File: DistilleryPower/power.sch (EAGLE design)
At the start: 31 parts, among them IC2 ACS758LCB-050B-PFF-T, J1 GREEN-2P-5.0, J2 GREEN-2P-5.0, Q1 BC807-16LT1SMD, T1 BT138-DSH, U1 STM32F042KXTX

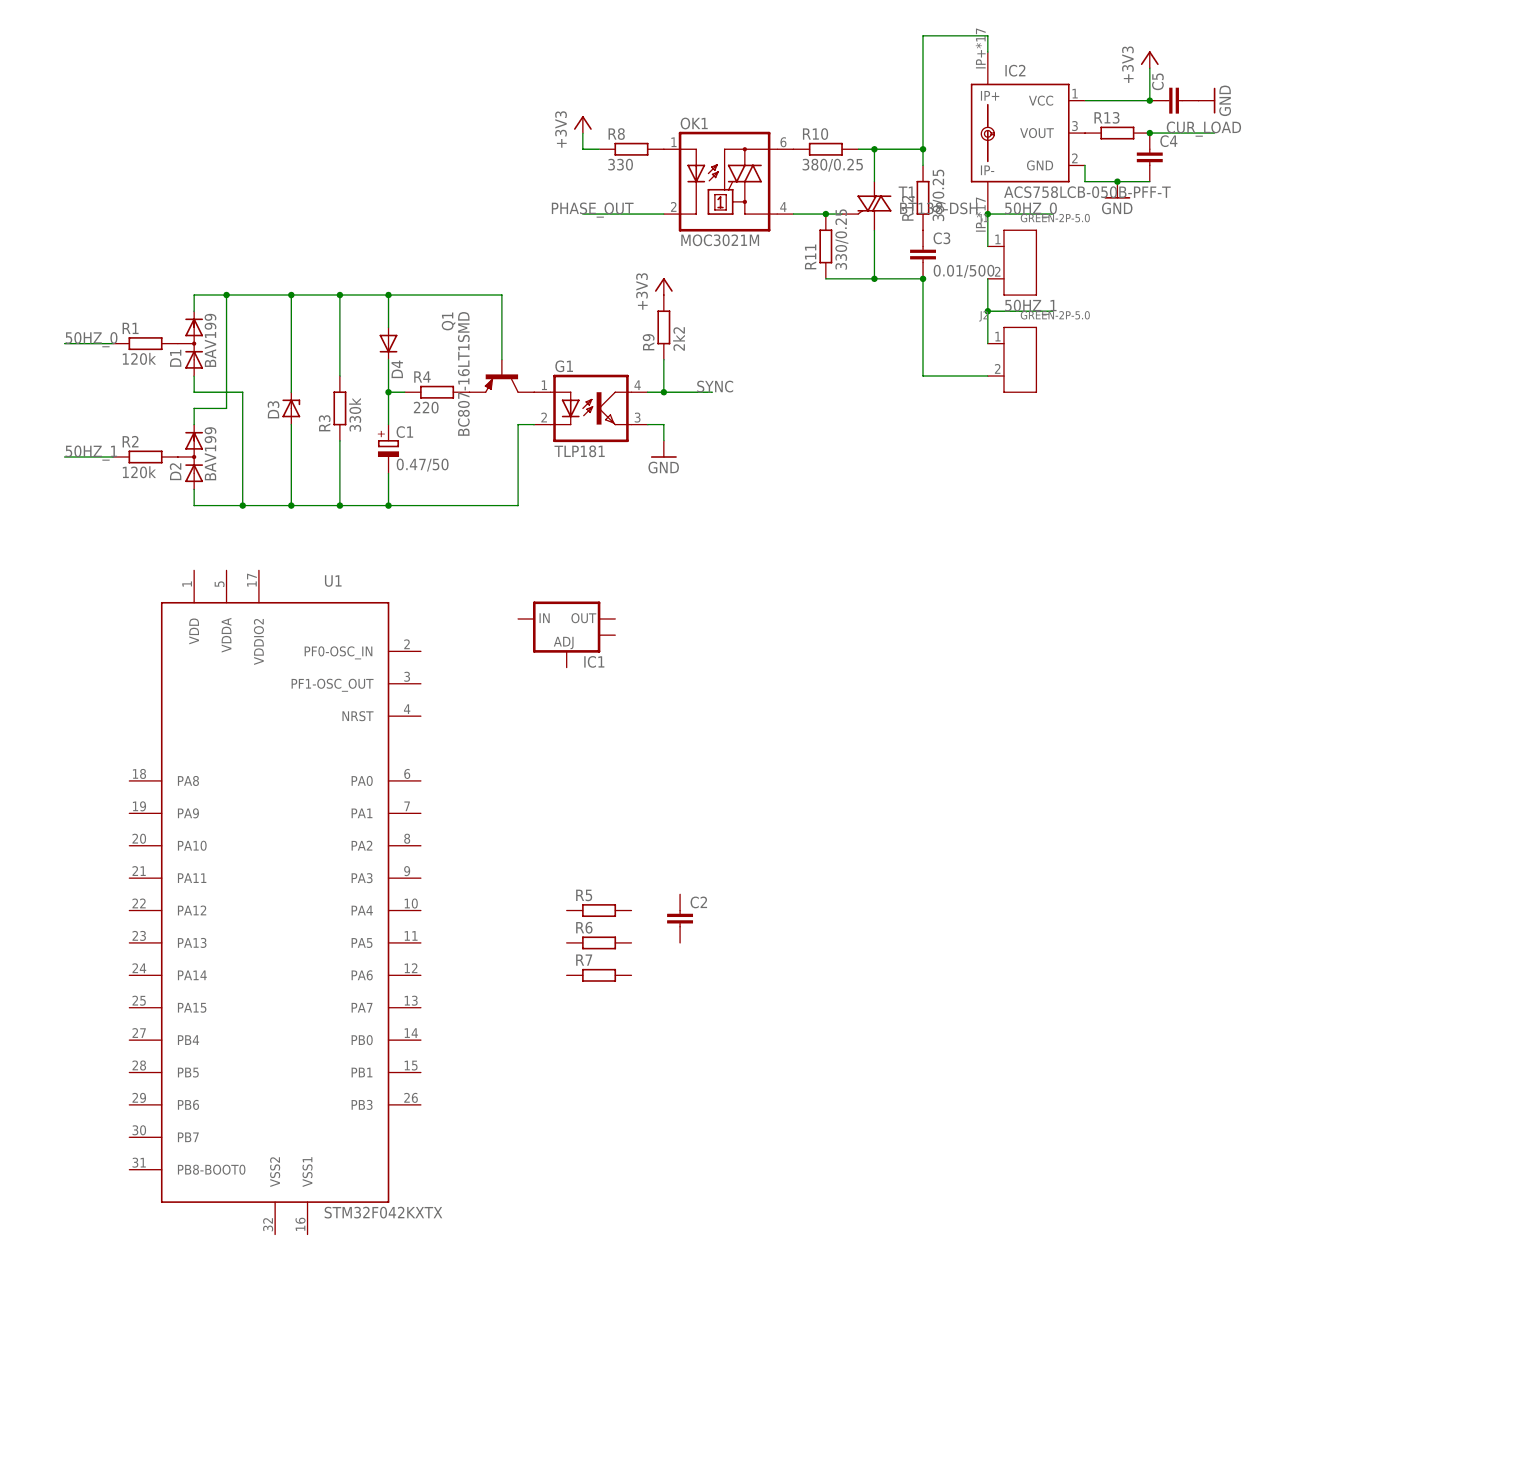
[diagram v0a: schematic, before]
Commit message: digital part schematics
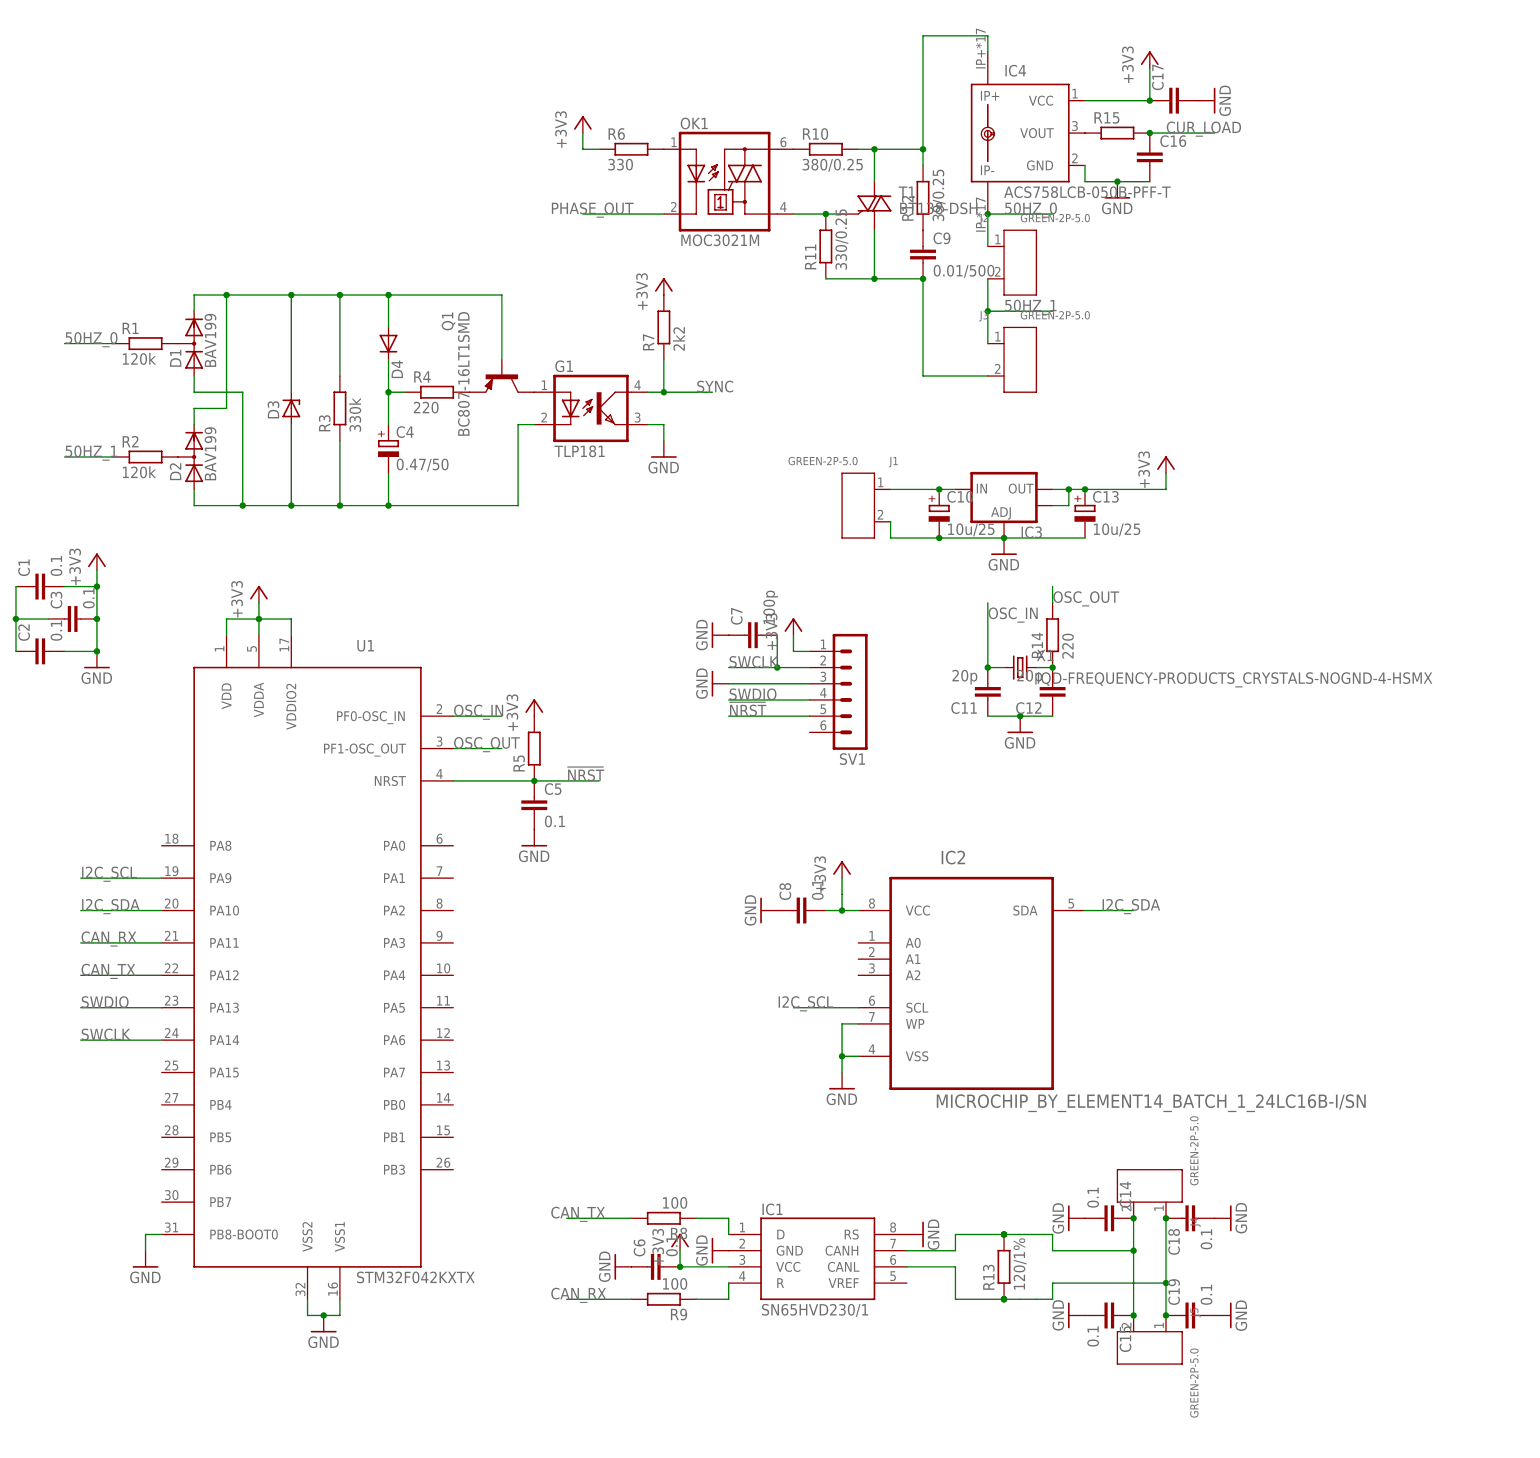
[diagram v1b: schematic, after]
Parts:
- added C10, C13: 10u/25, rcl:CPOL-EUSMCB
- added C11, C12: 20p, rcl:C-EUC0805
- added C14, C15, C18, C19, C6, C8: 0.1, rcl:C-EUC0805
- added C16, C17: (no value), rcl:C-EUC0805
- added C7: 100p, rcl:C-EUC0805
- added C9: 0.01/500, rcl:C-EUC1206
- added IC3: (no value), SparkFun:V_REG_LM1117SOT223
- added IC4: ACS758LCB-050B-PFF-T, allegro:ACS758LCB-050B-PFF-T
- added J3, J4, J5: GREEN-2P-5.0, distillery:SCREW-TERMINAL-GREEN(2P-5.0)
- added R14: 220, rcl:R-EU_R0805
- added R15: (no value), rcl:R-EU_R0805
- added SV1: (no value), distillery:CON-LSTB_MA06-1
- added X1: IQD-FREQUENCY-PRODUCTS_CRYSTALS-NOGND-4-HSMX, distillery:IQD-FREQUENCY-PRODUCTS_CRYSTALS-NOGND-4-HSMX
- C1: value 0.47/50 -> 0.1; device rcl:CPOL-EUC/6032-28R -> rcl:C-EUC0805
- C2, C5: value (none) -> 0.1
- C3: value 0.01/500 -> 0.1; device rcl:C-EUC1206 -> rcl:C-EUC0805
- C4: value (none) -> 0.47/50; device rcl:C-EUC0805 -> rcl:CPOL-EUC/6032-28R
- IC1: value (none) -> SN65HVD230/1; device SparkFun:V_REG_LM1117SOT223 -> distillery:SN65HVD230/1
- IC2: value ACS758LCB-050B-PFF-T -> MICROCHIP_BY_ELEMENT14_BATCH_1_24LC16B-I/SN; device allegro:ACS758LCB-050B-PFF-T -> distillery:MICROCHIP_BY_ELEMENT14_BATCH_1_24LC16B-I/SN
- R13: value (none) -> 120/1%
- R6: value (none) -> 330
- R7: value (none) -> 2k2
- R8: value 330 -> 100
- R9: value 2k2 -> 100
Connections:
- new net !NRST: C5.1, R5.1, SV1.5, U1.NRST
- new net CAN_RX: R9.2, U1.PA11
- new net CAN_TX: R8.2, U1.PA12
- new net I2C_SCL: IC2.SCL, U1.PA9
- new net I2C_SDA: IC2.SDA, U1.PA10
- new net N$13: C10.+, IC3.IN, J1.1
- new net N$16: C12.2, R14.1, X1.2
- new net N$19: C1.1, C2.1, C3.1
- new net N$20: C18.1, C19.1, IC1.CANL, J4.1, J5.1, R13.1
- new net N$21: IC1.D, R8.1
- new net N$22: IC1.R, R9.1
- new net N$24: C14.1, C15.1, IC1.CANH, J4.2, J5.2, R13.2
- new net OSC_IN: C11.2, U1.PF0-OSC_IN, X1.1
- new net OSC_OUT: R14.2, U1.PF1-OSC_OUT
- new net SWCLK: C7.2, SV1.2, U1.PA14
- new net SWDIO: SV1.4, U1.PA13
- net +3V3: now also C13.+, C17.1, C6.2, C8.2, IC1.VCC, IC3.OUT, IC3.OUT@1, IC4.VCC, R5.2, R6.1, R7.2, SV1.1, U1.VDD, U1.VDDA, U1.VDDIO2; no longer C5.1, R8.1, R9.2
- net 50HZ_0: now also IC4.IP-, J2.1; no longer IC2.IP-, J1.1
- net 50HZ_1: now also J2.2, J3.1; no longer J1.2, J2.1
- net CUR_LOAD: now also C16.1, R15.2; no longer C4.1, R13.2
- net GND: now also C1.2, C10.-, C11.1, C12.1, C13.-, C14.2, C15.2, C16.2, C17.2, C18.2, C19.2, C2.2, C3.2, C6.1, C7.1, C8.1, IC1.GND, IC1.RS, IC2.VSS, IC2.WP, IC3.ADJ, IC4.GND, J1.2, SV1.3, U1.PB8-BOOT0, U1.VSS1, U1.VSS2; no longer C4.2, IC2.GND
- net N$10: now also C9.1; no longer C3.1
- net N$14: now also R6.2; no longer R8.2
- net N$17: now also IC4.IP+; no longer IC2.IP+
- net N$18: now also C9.2, J3.2; no longer C3.2, J2.2
- net N$2: now also IC4.VOUT, R15.1; no longer IC2.VOUT, R13.1
- net N$5: now also C4.-; no longer C1.-
- net N$6: now also C4.+; no longer C1.+
- net SYNC: now also R7.1; no longer R9.1
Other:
- moved on the sheet: C2, C3, C5, J1, J2, R13, R5, R6, R7, R8, R9, U1

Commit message: power control board routing finished
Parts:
- added C20, C21: 0.1, rcl:C-EUC0603
- added R16, R17, R18, R19, R20, R21, R22, R23, R24, R25, R26: 100, rcl:R-EU_R0603
- added X2: 2516-, con-3m:2516-
- C1, C11, C12, C14, C15, C16, C17, C18, C19, C2, C3, C5, C6, C7, C8: device rcl:C-EUC0805 -> rcl:C-EUC0603
- R13, R14, R15, R5, R6, R7, R8, R9: device rcl:R-EU_R0805 -> rcl:R-EU_R0603
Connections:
- removed net N$19: C1.1, C2.1, C3.1
- removed net SYNC: G1.COL, R7.1
- new net A: R16.1, U1.PA0
- new net B: R17.1, U1.PA1
- new net C: R18.1, U1.PA2
- new net D: R19.1, U1.PA3
- new net DG0: R24.1, U1.PB4
- new net DG1: R25.1, U1.PB5
- new net DG2: R26.1, U1.PB6
- new net DP: R23.1, U1.PA7
- new net E: R20.1, U1.PA4
- new net F: R21.1, U1.PA5
- new net G: R22.1, U1.PA6
- new net N$15: R16.2, X2-3.KL
- new net N$23: R17.2, X2-4.KL
- new net N$25: R18.2, X2-5.KL
- new net N$26: R19.2, X2-6.KL
- new net N$27: R20.2, X2-7.KL
- new net N$28: R21.2, X2-8.KL
- new net N$29: R22.2, X2-9.KL
- new net N$30: R23.2, X2-10.KL
- new net N$31: R24.2, X2-11.KL
- new net N$32: R25.2, X2-12.KL
- new net N$33: R26.2, X2-13.KL
- new net SW0: C20.2, U1.PB0, X2-14.KL
- new net SW1: C21.2, U1.PA8, X2-15.KL
- new net ZERO_CROSS: G1.COL, R7.1, U1.PB7
- net +3V3: now also C1.2, C2.2, C3.2, X2-2.KL; no longer R6.1
- net CUR_LOAD: now also U1.PB1
- net GND: now also C1.1, C2.1, C20.1, C21.1, C3.1, J1.1, R6.1, X2-1.KL, X2-16.KL; no longer C1.2, C2.2, C3.2, J1.2
- net N$13: now also J1.2; no longer J1.1
- net N$14: now also OK1.C; no longer OK1.A
- net N$20: now also C14.1, C15.1, J4.2, J5.2; no longer C18.1, C19.1, J4.1, J5.1
- net N$24: now also C18.1, C19.1, J4.1, J5.1; no longer C14.1, C15.1, J4.2, J5.2
- net PHASE_OUT: now also OK1.A, U1.PA15; no longer OK1.C
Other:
- moved on the sheet: C1, C2, C3, J1, R6
